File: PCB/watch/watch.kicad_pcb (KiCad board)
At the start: 2 copper layers, 1 part

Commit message: feat(pcb): Buncha stuff happened
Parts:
- removed the REF** at (150.0, 100.0)
- added REF**: Val**, Casio Footprints:CASIO-F91W-OUTLINE, F.Cu at (150.0, 100.0)
- added REF**: Crystal_SMD_3225-4Pin_3.2x2.5mm, Crystal:Crystal_SMD_3225-4Pin_3.2x2.5mm, F.Cu at (142.5, 104.5)
- added REF**: LQFP48-7X7mm, STM8S105C6T6:LQFP48-7X7mm, F.Cu at (151.2, 104.2)
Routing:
- net (no net): track 0.00 -> 381.4 mm, vias 0 -> 10
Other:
- board outline added: 24.4 x 24.4 mm
- copper layers 2 -> 4
- board text added: "JLCJLCJLCJLC"
- board text added: "Project C Devboard V0.1"

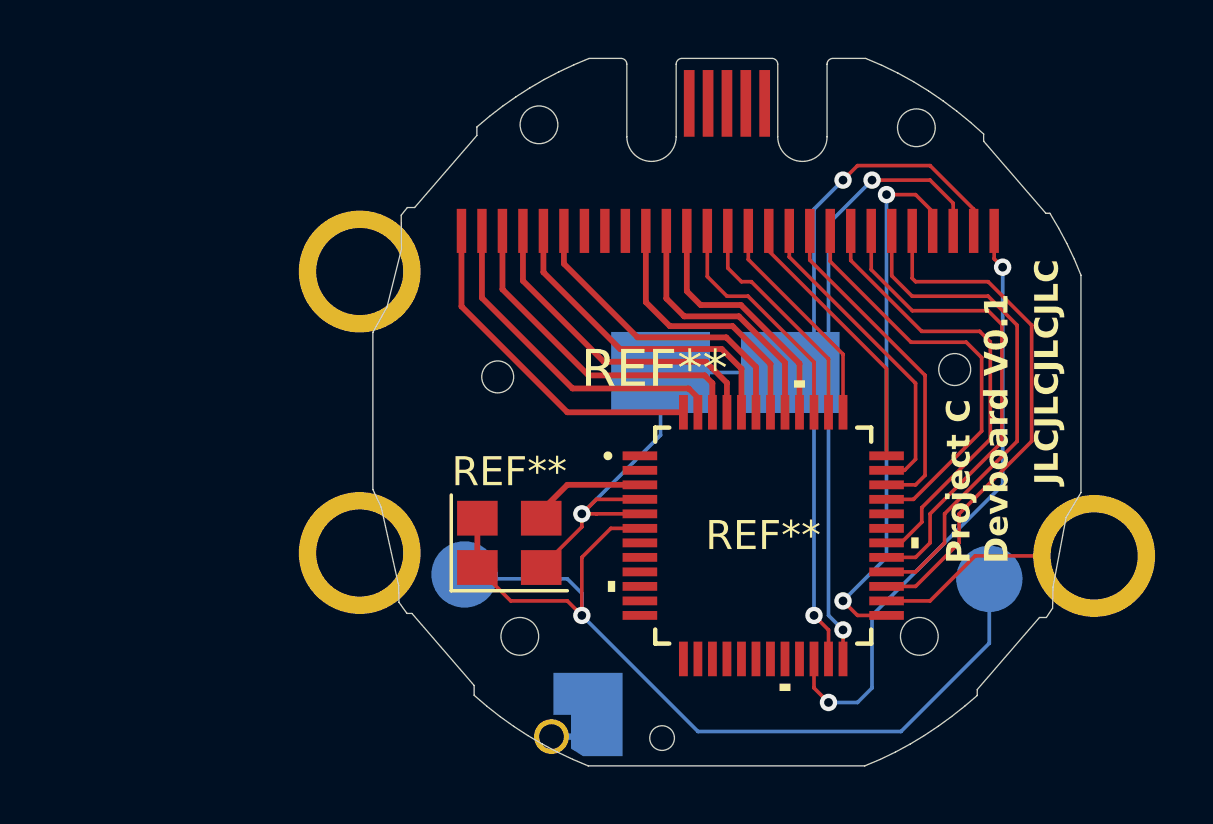
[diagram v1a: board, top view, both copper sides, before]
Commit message: refactor(pcb): Turns out diagonal is better
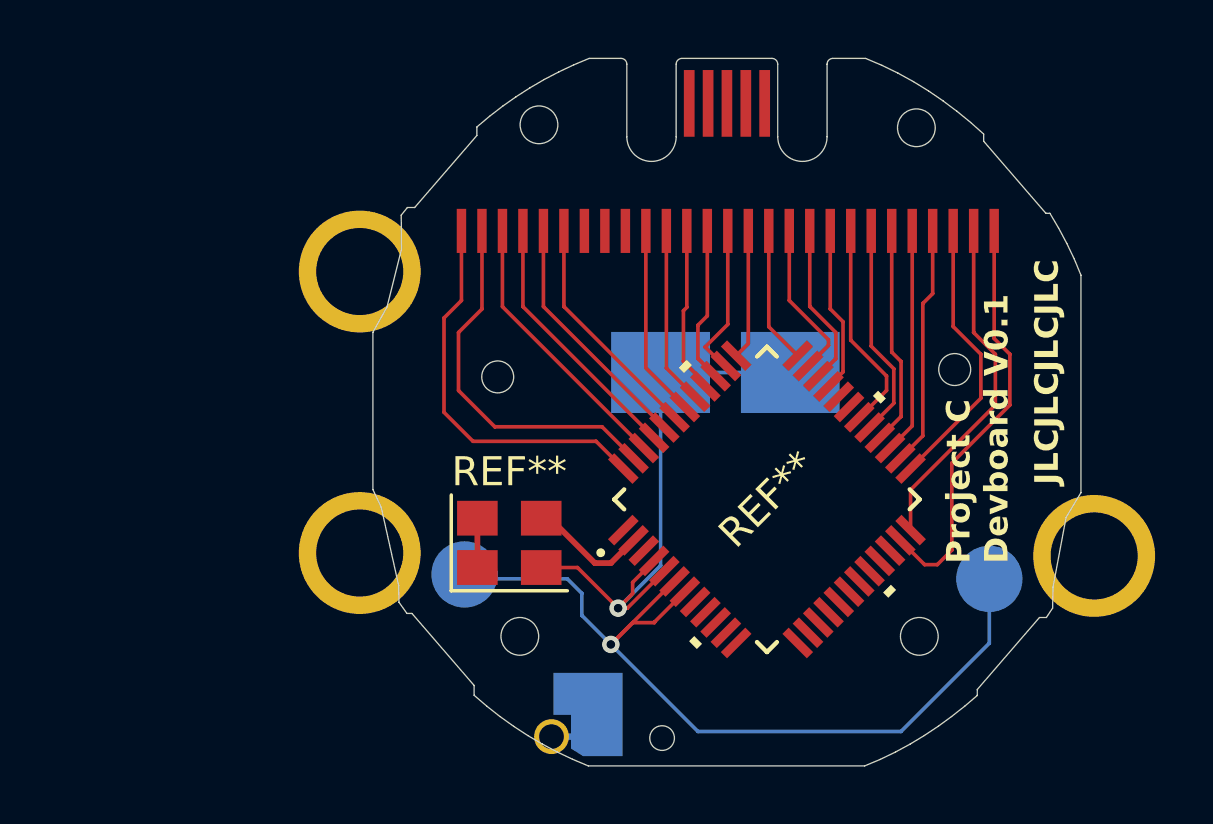
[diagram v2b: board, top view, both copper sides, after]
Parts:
- moved REF** 1.26 mm to (151.4, 103.0), turned to 45 degrees
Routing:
- net (no net): track 381.4 -> 249.1 mm, vias 10 -> 2

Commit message: feat: Even more stuff
I'm pretty shure the CP2102 isnt even used. But its there I guess.
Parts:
- added REF**: LED_WS2812B-Mini_PLCC4_3.5x3.5mm, LED_SMD:LED_WS2812B-Mini_PLCC4_3.5x3.5mm, F.Cu at (129.0, 99.2)
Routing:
- net (no net): track 249.1 -> 331.4 mm, vias 2 -> 6
